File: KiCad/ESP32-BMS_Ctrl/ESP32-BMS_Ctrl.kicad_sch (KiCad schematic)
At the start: 44 parts, among them J1 Screw_Terminal_01x02, J2 Screw_Terminal_01x02, J3 Screw_Terminal_01x02, J4 Conn_01x02, J5 Conn_01x02, J6 DE9_Receptacle_MountingHoles, J7 Screw_Terminal_01x02, Q1 IRF4905PBF, Q2 IRF4905PBF, Q3 IRF4905PBF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

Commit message: minor updates on main PCB
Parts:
- J4, J5: footprint Connector_JST:JST_XH_B2B-XH-AM_1x02_P2.50mm_Vertical -> Connector_JST:JST_XH_B2B-XH-A_1x02_P2.50mm_Vertical
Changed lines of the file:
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@@
       (effects (font (size 1.27 1.27)) (justify left))
     )
-    (property "Footprint" "Connector_JST:JST_XH_B2B-XH-AM_1x02_P2.50mm_Vertical" (at 161.29 162.56 0)
+    (property "Footprint" "Connector_JST:JST_XH_B2B-XH-A_1x02_P2.50mm_Vertical" (at 161.29 162.56 0)
       (effects (font (size 1.27 1.27)) hide)
     )
@@
       (effects (font (size 1.27 1.27)) (justify left))
     )
-    (property "Footprint" "Connector_JST:JST_XH_B2B-XH-AM_1x02_P2.50mm_Vertical" (at 161.29 113.03 0)
-      (effects (font (size 1.27 1.27)) hide)
-    )
+    (property "Footprint" "Connector_JST:JST_XH_B2B-XH-A_1x02_P2.50mm_Vertical" (at 161.29 113.03 0)
+      (effects (font (size 1.27 1.27)) hide)
+    )

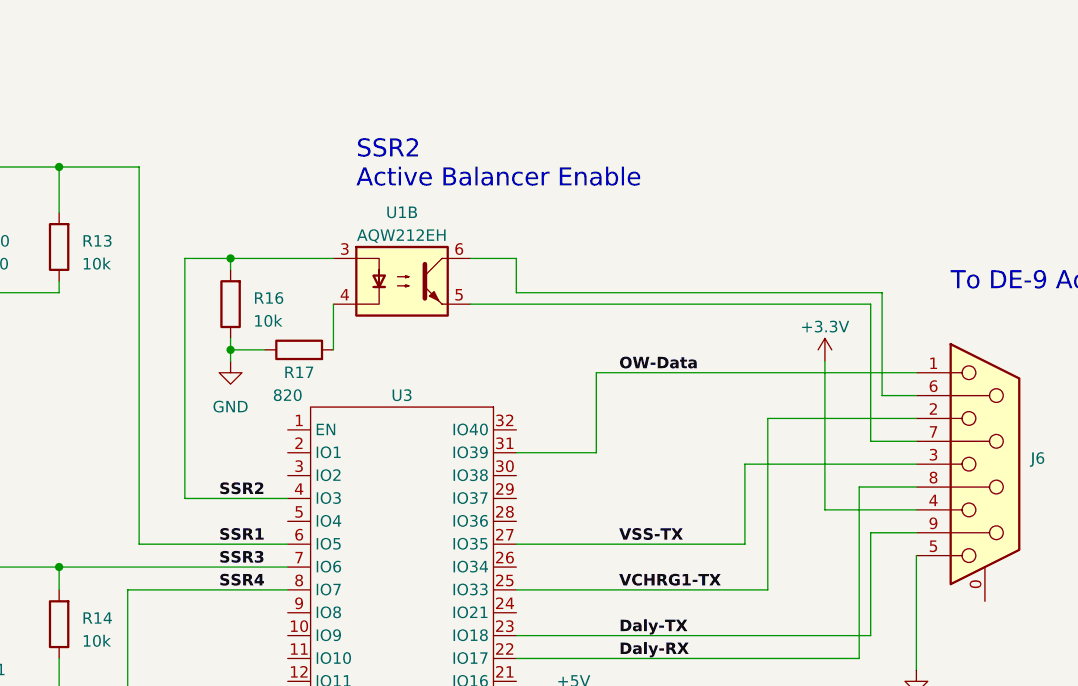
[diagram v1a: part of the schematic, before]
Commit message: OneWire working now; updated KiCad data
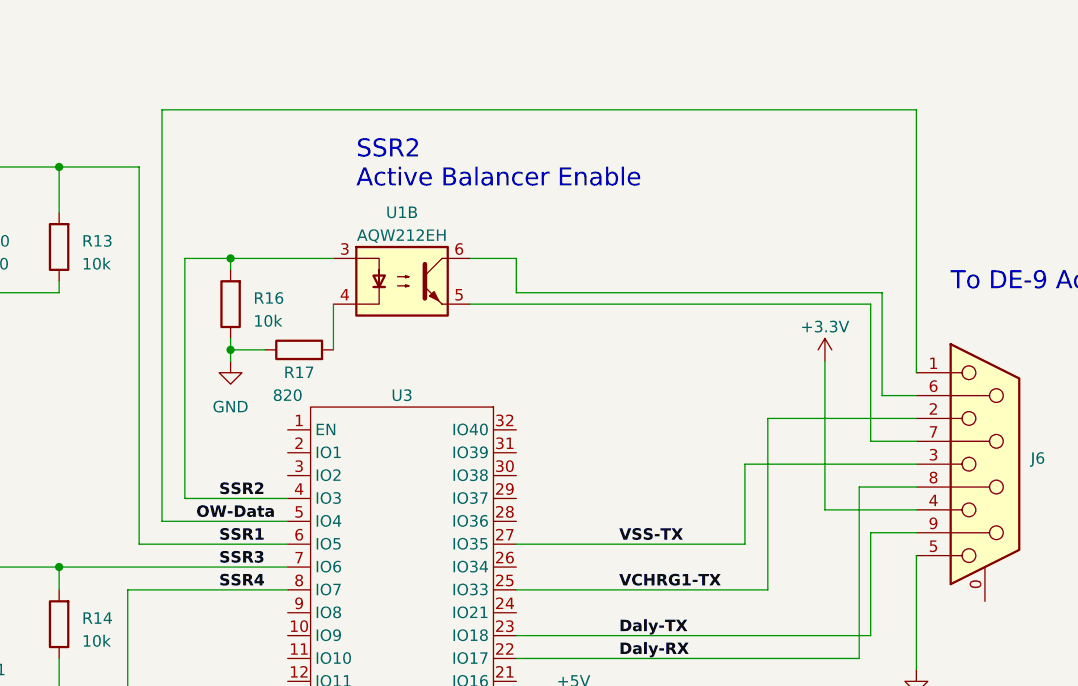
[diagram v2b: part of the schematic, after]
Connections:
- net OW-Data: now also U3.5 (IO4); no longer U3.31 (IO39)
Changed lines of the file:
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@@
   (junction (at 73.66 163.83) (diameter 0) (color 0 0 0 0)
   )
+  (wire (pts (xy 281.94 67.31) (xy 281.94 38.1))
+    (stroke (width 0) (type default))
+  )
   (wire (pts (xy 276.86 96.52) (xy 276.86 85.09))
     (stroke (width 0) (type default))
@@
     (stroke (width 0) (type default))
   )
+  (wire (pts (xy 198.12 83.82) (xy 212.09 83.82))
+    (stroke (width 0) (type default))
+  )
   (wire (pts (xy 137.16 138.43) (xy 137.16 143.51))
     (stroke (width 0) (type default))
@@
     (stroke (width 0) (type default))
   )
-  (wire (pts (xy 246.38 76.2) (xy 237.49 76.2))
-    (stroke (width 0) (type default))
-  )
   (wire (pts (xy 355.6 179.07) (xy 367.03 179.07))
     (stroke (width 0) (type default))
@@
     (stroke (width 0) (type default))
   )
+  (wire (pts (xy 198.12 38.1) (xy 198.12 83.82))
+    (stroke (width 0) (type default))
+  )
   (wire (pts (xy 83.82 55.88) (xy 92.71 55.88))
     (stroke (width 0) (type default))
@@
     (stroke (width 0) (type default))
   )
+  (wire (pts (xy 281.94 38.1) (xy 198.12 38.1))
+    (stroke (width 0) (type default))
+  )
   (wire (pts (xy 194.31 91.44) (xy 194.31 147.32))
     (stroke (width 0) (type default))
@@
     (stroke (width 0) (type default))
   )
-  (wire (pts (xy 246.38 67.31) (xy 246.38 76.2))
-    (stroke (width 0) (type default))
-  )
   (wire (pts (xy 83.82 48.26) (xy 83.82 55.88))
     (stroke (width 0) (type default))
@@
   )
   (wire (pts (xy 175.26 58.42) (xy 175.26 60.96))
-    (stroke (width 0) (type default))
-  )
-  (wire (pts (xy 246.38 67.31) (xy 281.94 67.31))
     (stroke (width 0) (type default))
   )
@@
     (effects (font (size 1.27 1.27) bold) (justify left bottom))
   )
-  (label "OW-Data" (at 248.92 67.31 0) (fields_autoplaced)
+  (label "OW-Data" (at 201.93 83.82 0) (fields_autoplaced)
     (effects (font (size 1.27 1.27) bold) (justify left bottom))
   )
